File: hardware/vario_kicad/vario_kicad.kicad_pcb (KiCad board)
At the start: 4 copper layers, 70 x 50 mm, 93 parts, among them Q1 NMOS, Q2 PMOS, U2 BME280, U3 W25Q128JVS, U4 USB C connector, U5 STM32L072CBTx, Y1 Crystal, Y2 Crystal_GND24

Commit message: finalize v2 layout
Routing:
- net Net-(U3-CLK): track 15.5 -> 14.2 mm
- net GND: vias 35 -> 38
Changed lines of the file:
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@@
+	)
+	(via
+		(at 124.47 123.8)
+		(size 0.5)
+		(drill 0.3)
+		(layers "F.Cu" "B.Cu")
+		(free yes)
+		(net 2)
 	)
 	(via
@@
 	)
 	(via
+		(at 142.16 115.65)
+		(size 0.5)
+		(drill 0.3)
+		(layers "F.Cu" "B.Cu")
+		(free yes)
+		(net 2)
+	)
+	(via
 		(at 152.01 129.4)
 		(size 0.5)
@@
 		(drill 0.3)
 		(layers "F.Cu" "B.Cu")
+		(net 2)
+	)
+	(via
+		(at 122.64 120.94)
+		(size 0.5)
+		(drill 0.3)
+		(layers "F.Cu" "B.Cu")
+		(free yes)
 		(net 2)
 	)
@@
 	)
 	(segment
-		(start 131.83 117.87)
-		(end 131.83 116.2)
+		(start 131.81 116.29)
+		(end 131.04 115.52)
 		(width 0.2)
 		(layer "F.Cu")
@@
 	)
 	(segment
-		(start 131.15 115.52)
+		(start 124.55 124.56)
+		(end 131.81 117.3)
+		(width 0.2)
+		(layer "F.Cu")
+		(net 42)
+	)
+	(segment
+		(start 131.81 117.3)
+		(end 131.81 116.29)
+		(width 0.2)
+		(layer "F.Cu")
+		(net 42)
+	)
+	(segment
+		(start 131.04 115.52)
 		(end 129.95 115.52)
 		(width 0.2)
@@
 	(segment
 		(start 124.55 125.34)
-		(end 124.55 123.16)
-		(width 0.2)
-		(layer "F.Cu")
-		(net 42)
-	)
-	(segment
-		(start 124.55 123.16)
-		(end 129.52 118.19)
-		(width 0.2)
-		(layer "F.Cu")
-		(net 42)
-	)
-	(segment
-		(start 129.52 118.19)
-		(end 131.51 118.19)
-		(width 0.2)
-		(layer "F.Cu")
-		(net 42)
-	)
-	(segment
-		(start 131.51 118.19)
-		(end 131.83 117.87)
-		(width 0.2)
-		(layer "F.Cu")
-		(net 42)
-	)
-	(segment
-		(start 131.83 116.2)
-		(end 131.15 115.52)
-		(width 0.2)
-		(layer "F.Cu")
+		(end 124.55 124.56)
+		(width 0.2)
+		(layer "F.Cu")

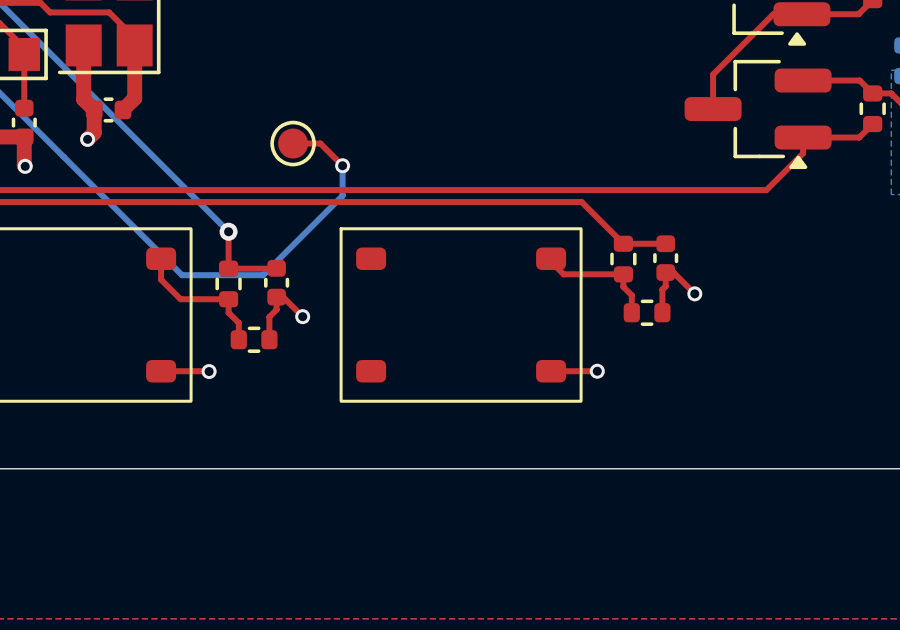
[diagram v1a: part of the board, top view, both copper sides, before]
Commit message: make switches symmetrical
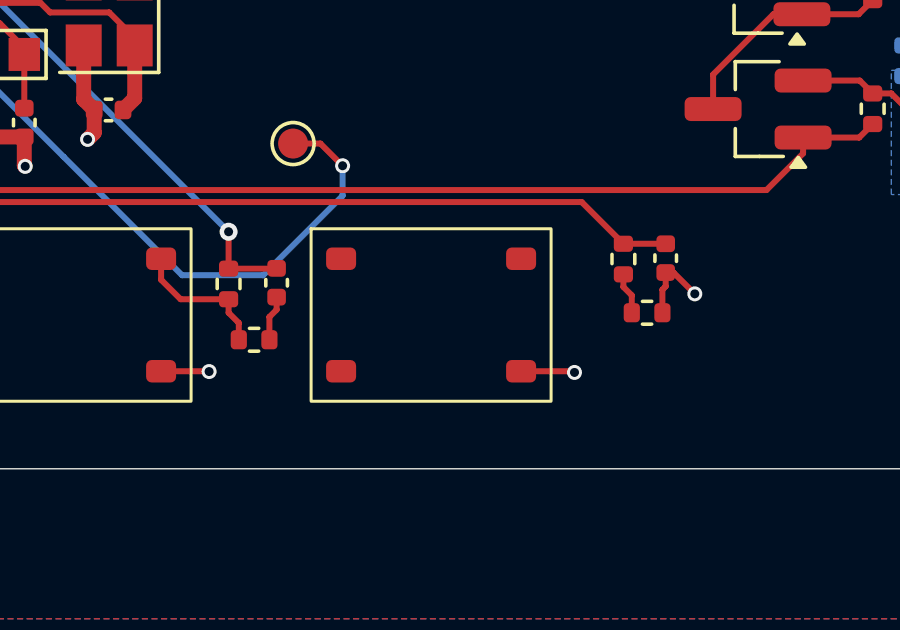
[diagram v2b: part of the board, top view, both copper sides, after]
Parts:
- moved S6 1.00 mm to (147.0, 143.0)
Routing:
- net Net-(S6-B): track 4.08 -> 1.40 mm
- net GND: track 85.2 -> 84.0 mm, vias 38 -> 37
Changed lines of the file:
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@@
 	(footprint "symbol_lib:TS-1187A-B-A-B_switch"
 		(layer "F.Cu")
-		(at 148 143)
+		(at 147 143)
 		(property "Reference" "S6"
 			(at 0 -7 0)
@@
 	)
 	(segment
-		(start 142.07 144.28)
-		(end 142.72 144.93)
-		(width 0.2)
-		(layer "F.Cu")
-		(net 2)
-	)
-	(segment
 		(start 107.455 121.48)
 		(end 107.455 120.985)
@@
 	)
 	(segment
-		(start 141.85 144.28)
-		(end 142.07 144.28)
-		(width 0.2)
-		(layer "F.Cu")
-		(net 2)
-	)
-	(segment
 		(start 137.12 133.69)
 		(end 139.09 133.69)
@@
 	)
 	(via
-		(at 142.72 144.93)
-		(size 0.5)
-		(drill 0.3)
-		(layers "F.Cu" "B.Cu")
-		(net 2)
-	)
-	(via
 		(at 165 138.5)
 		(size 0.5)
@@
 	)
 	(segment
+		(start 150 146.75)
+		(end 151.74 146.75)
+		(width 0.2)
+		(layer "F.Cu")
+		(net 3)
+	)
+	(segment
 		(start 120.05 128.775)
 		(end 119.065 128.775)
@@
 	)
 	(segment
-		(start 151 146.75)
-		(end 152.54 146.75)
-		(width 0.2)
-		(layer "F.Cu")
-		(net 3)
-	)
-	(segment
 		(start 107.03 115.47)
 		(end 108.12 114.38)
@@
 	)
 	(segment
+		(start 151.74 146.75)
+		(end 151.78 146.79)
+		(width 0.2)
+		(layer "F.Cu")
+		(net 3)
+	)
+	(segment
 		(start 129.95 112.98)
 		(end 131.87 112.98)
@@
 	)
 	(via
-		(at 126.57 136.68)
+		(at 151.78 146.79)
 		(size 0.5)
 		(drill 0.3)
 		(layers "F.Cu" "B.Cu")
-		(free yes)
 		(net 3)
 	)
 	(via
-		(at 152.54 146.75)
+		(at 126.57 136.68)
 		(size 0.5)
 		(drill 0.3)
 		(layers "F.Cu" "B.Cu")
+		(free yes)
 		(net 3)
 	)
@@
 		(width 0.2)
 		(layer "F.Cu")
-		(net 72)
-	)
-	(segment
-		(start 151 143.1)
-		(end 151.42 143.52)
-		(width 0.2)
-		(layer "F.Cu")
-		(net 72)
-	)
-	(segment
-		(start 151.42 143.52)
-		(end 153.41 143.52)
-		(width 0.2)
-		(layer "F.Cu")
-		(net 72)
-	)
-	(segment
-		(start 151 143)
-		(end 151 143.1)
-		(width 0.2)
-		(layer "F.Cu")

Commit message: design almost finished
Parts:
- added R33: 0R, Resistor_SMD:R_0402_1005Metric, B.Cu at (157.6, 121.1)
- R24, R25: value 220k -> 100k
- moved C28 0.43 mm to (154.5, 143.2)
- moved R40 0.43 mm to (153.1, 143.2)
- moved R37 0.43 mm to (153.8, 145.0)
- moved C17 0.16 mm to (141.7, 143.8)
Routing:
- net GND: track 84.0 -> 93.0 mm, vias 37 -> 44
- net VBATT: track 24.2 -> 28.2 mm
- net Net-(S6-B): track 1.40 -> 4.76 mm
- net V_USB: track 92.3 -> 93.8 mm
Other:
- rule pad_to_mask_clearance: 0.05 -> 0

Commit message: minor changes to layout
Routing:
- net GND: track 93.0 -> 93.3 mm, vias 44 -> 46
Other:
- board text added: "github.com/vasilNnikolov/vario R1.0"
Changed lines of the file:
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@@
 		(layer "Edge.Cuts")
+	)
+	(gr_text "github.com/vasilNnikolov/vario\nR1.0"
+		(at 136.28 146.31 0)
+		(layer "B.SilkS")
+		(effects
+			(font
+				(size 0.5 0.5)
+				(thickness 0.1)
+			)
+			(justify left bottom mirror)
+		)
 	)
 	(segment
@@
 	)
 	(segment
-		(start 107.99 116.11)
-		(end 107.99 116.82)
-		(width 0.2)
-		(layer "F.Cu")
-		(net 2)
-	)
-	(segment
 		(start 154.46 143.69)
 		(end 154.46 144.15)
@@
 	)
 	(segment
+		(start 155.53 143.69)
+		(end 155.54 143.7)
+		(width 0.2)
+		(layer "F.Cu")
+		(net 2)
+	)
+	(segment
 		(start 154.35 144.26)
 		(end 154.35 145.03)
@@
 	)
 	(segment
+		(start 154.46 143.69)
+		(end 155.53 143.69)
+		(width 0.2)
+		(layer "F.Cu")
+		(net 2)
+	)
+	(segment
 		(start 114.750589 141.669411)
 		(end 115.61 140.81)
@@
 	)
 	(segment
-		(start 154.46 143.69)
-		(end 154.72 143.69)
-		(width 0.2)
-		(layer "F.Cu")
-		(net 2)
-	)
-	(segment
 		(start 108.71 116.11)
 		(end 109.4 116.11)
@@
 	)
 	(segment
-		(start 154.72 143.69)
-		(end 155.43 144.4)
-		(width 0.2)
-		(layer "F.Cu")
-		(net 2)
-	)
-	(segment
 		(start 118.37 102.87)
 		(end 118.36 102.88)
@@
 	)
 	(segment
+		(start 107.99 116.11)
+		(end 107.99 117.23)
+		(width 0.2)
+		(layer "F.Cu")
+		(net 2)
+	)
+	(segment
 		(start 141.69 145.62)
 		(end 141.61 145.7)
@@
 	)
 	(segment
-		(start 107.99 116.82)
-		(end 107.64 117.17)
-		(width 0.2)
-		(layer "F.Cu")
-		(net 2)
-	)
-	(segment
 		(start 125.05 138.43)
 		(end 124.8 138.68)
@@
 	)
 	(via
+		(at 107.99 117.23)
+		(size 0.5)
+		(drill 0.3)
+		(layers "F.Cu" "B.Cu")
+		(net 2)
+	)
+	(via
 		(at 123.22 118.5)
 		(size 0.5)
@@
 	)
 	(via
-		(at 107.64 117.17)
-		(size 0.5)
-		(drill 0.3)
-		(layers "F.Cu" "B.Cu")
-		(net 2)
-	)
-	(via
 		(at 133.56 128.57)
 		(size 0.5)
@@
 	)
 	(via
-		(at 155.43 144.4)
-		(size 0.5)
-		(drill 0.3)
-		(layers "F.Cu" "B.Cu")
-		(net 2)
-	)
-	(via
 		(at 166 140.5)
 		(size 0.5)
@@
 	)
 	(via
+		(at 142.86 119.3)
+		(size 0.5)
+		(drill 0.3)
+		(layers "F.Cu" "B.Cu")
+		(net 2)
+	)
+	(via
 		(at 164 140.5)
 		(size 0.5)
@@
 	)
 	(via
-		(at 142.16 115.65)
+		(at 142.51 115.08)
 		(size 0.5)
 		(drill 0.3)
@@
 	)
 	(via
+		(at 155.54 143.7)
+		(size 0.5)
+		(drill 0.3)
+		(layers "F.Cu" "B.Cu")
+		(net 2)
+	)
+	(via
 		(at 123.51 102.87)
 		(size 0.5)
@@
 		(drill 0.3)
 		(layers "F.Cu" "B.Cu")
+		(net 2)
+	)
+	(via
+		(at 144.94 139.89)
+		(size 0.5)
+		(drill 0.3)
+		(layers "F.Cu" "B.Cu")
+		(free yes)
 		(net 2)
 	)
@@
 	(segment
 		(start 143.47 119.3)
+		(end 142.86 119.3)
+		(width 0.2)
+		(layer "B.Cu")
+		(net 2)
+	)
+	(segment
+		(start 143.47 119.3)
 		(end 144.16 119.99)
 		(width 0.2)
@@
 	(via
 		(at 140.25 142.1)
-		(size 0.6)
-		(drill 0.3)
-		(layers "F.Cu" "B.Cu")
+		(size 0.5)
+		(drill 0.3)
+		(layers "F.Cu" "B.Cu")

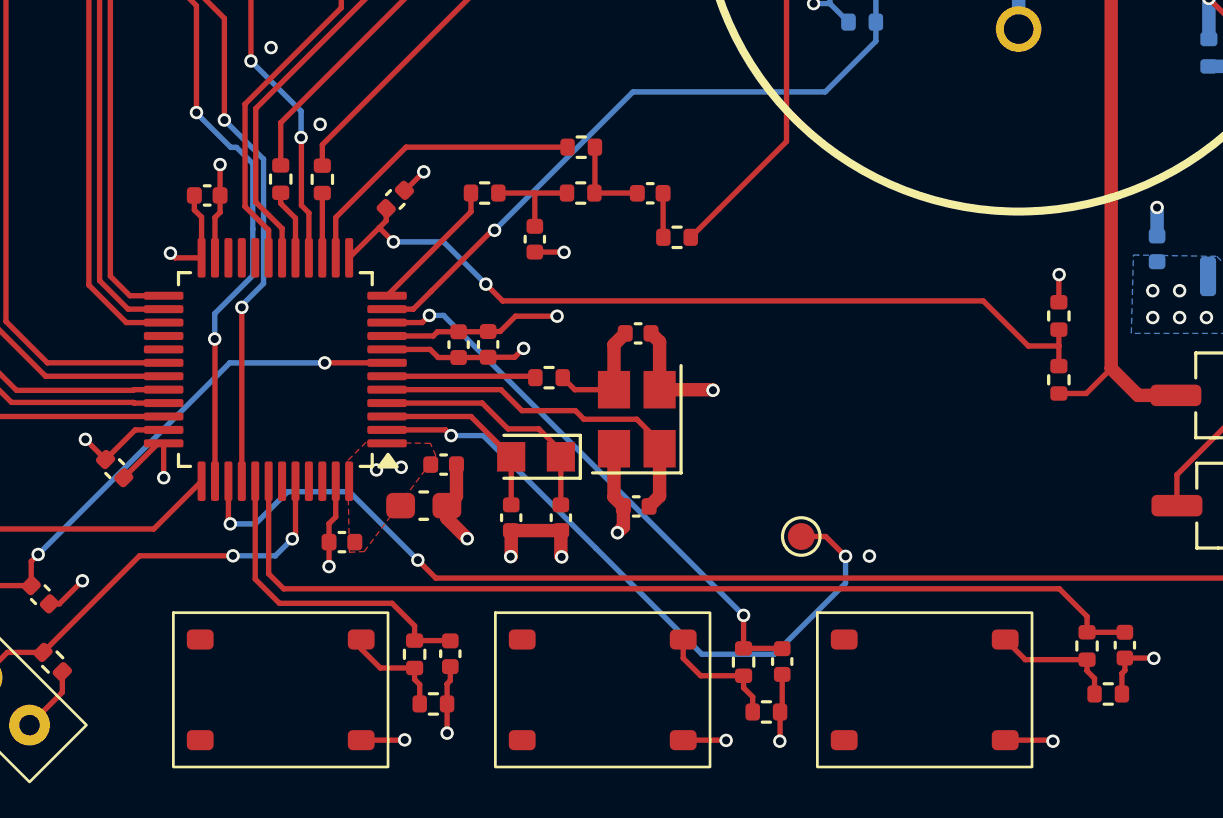
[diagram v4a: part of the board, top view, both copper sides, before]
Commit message: move LSE to bottom of board, move HSE closer to MCU
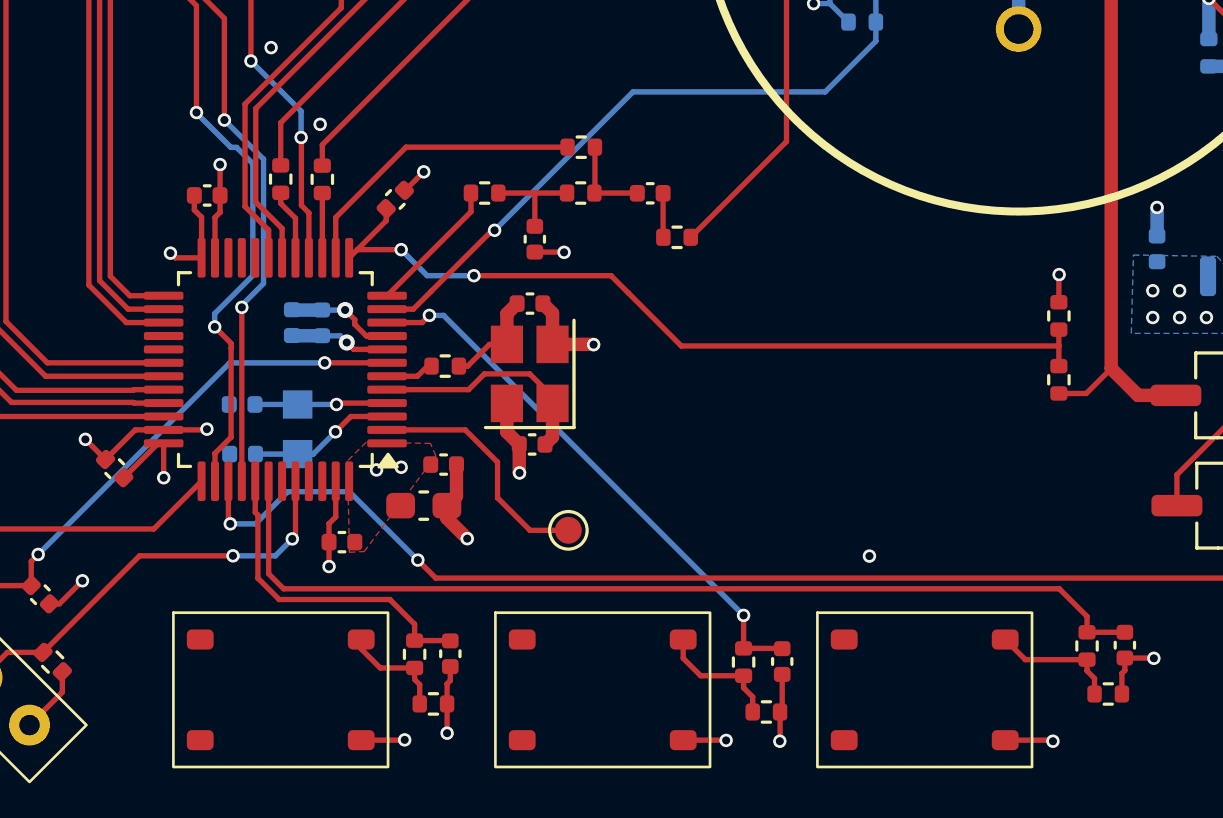
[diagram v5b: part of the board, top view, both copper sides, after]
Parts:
- C11, C25, C26, C27, Y1: moved to B.Cu
- moved C27 12.6 mm to (121.6, 134.2), turned to 180 degrees
- moved C26 10.3 mm to (121.6, 136.1), turned to 180 degrees
- moved Y1 8.94 mm to (123.6, 135.2), turned to -90 degrees
- moved TP4 8.68 mm to (133.7, 138.9)
- moved C25 7.34 mm to (123.4, 131.2)
- moved C11 5.16 mm to (124.5, 131.2)
- moved C13 4.52 mm to (132.4, 135.7)
- moved Y2 4.33 mm to (132.3, 133.1)
- moved C20 4.18 mm to (132.3, 130.5)
- moved R30 3.89 mm to (129.1, 132.8)
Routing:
- net /mcu/RTC_CALIB: track 24.6 -> 9.09 mm, vias 2 -> 0
- net GND: track 93.3 -> 87.9 mm, vias 46 -> 45
- net /mcu/OSC_IN: track 13.5 -> 8.66 mm
- net /mcu/OSC32_OUT: track 9.23 -> 4.94 mm, vias 0 -> 1
- net /mcu/OSC_OUT: track 5.55 -> 1.81 mm
- net VCC: track 49.4 -> 46.9 mm
- net /mcu/OSC32_IN: track 7.04 -> 5.48 mm, vias 0 -> 1
- net Net-(C20-Pad1): track 4.37 -> 3.80 mm
